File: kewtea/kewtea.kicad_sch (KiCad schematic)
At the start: 61 parts, among them U1 Nice_Nano_V2

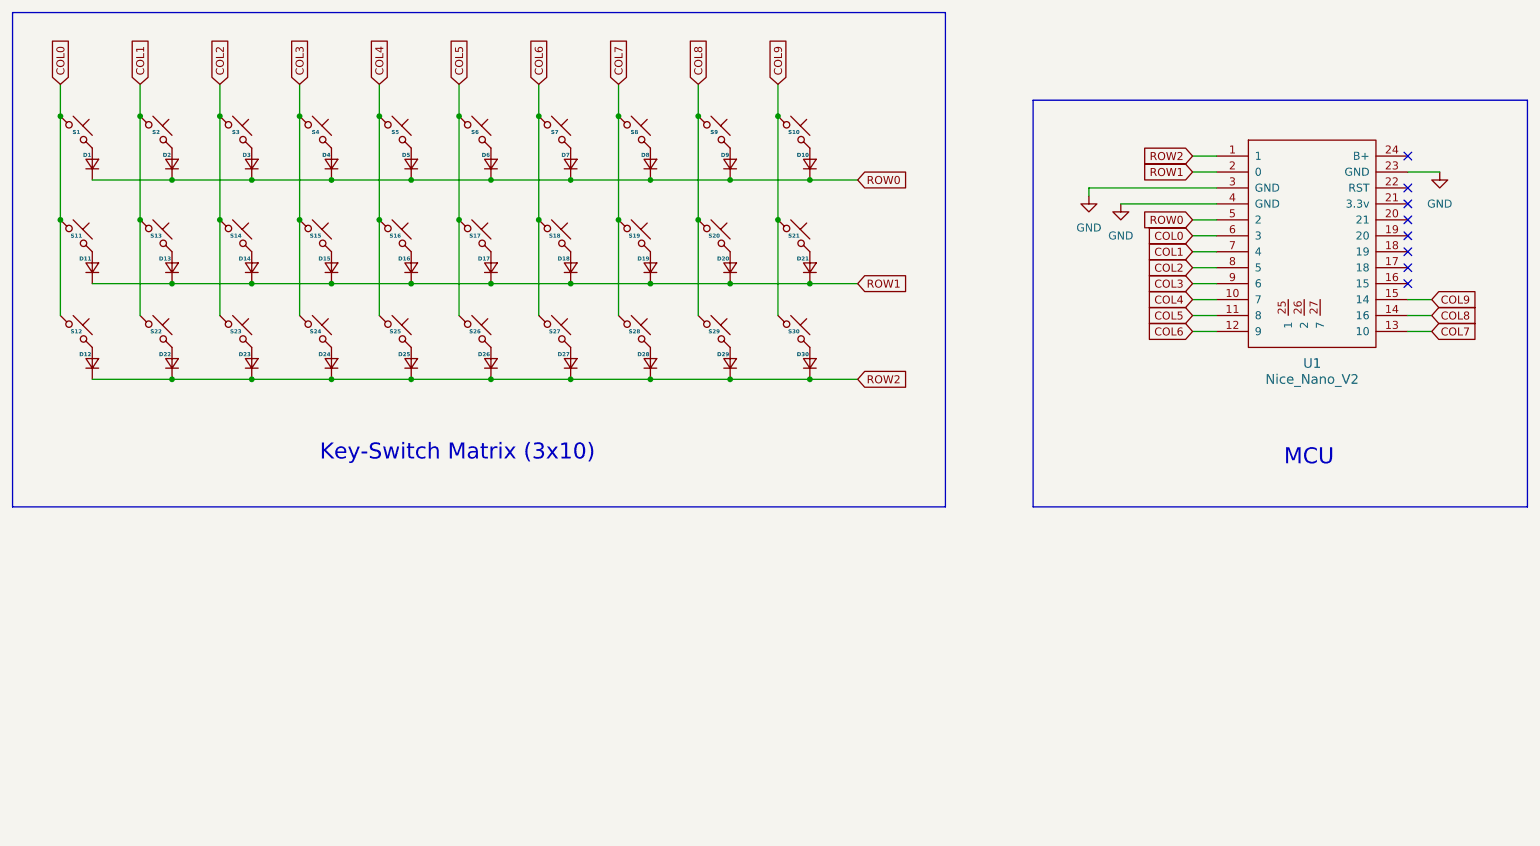
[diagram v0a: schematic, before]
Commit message: add pcb with 3d renders
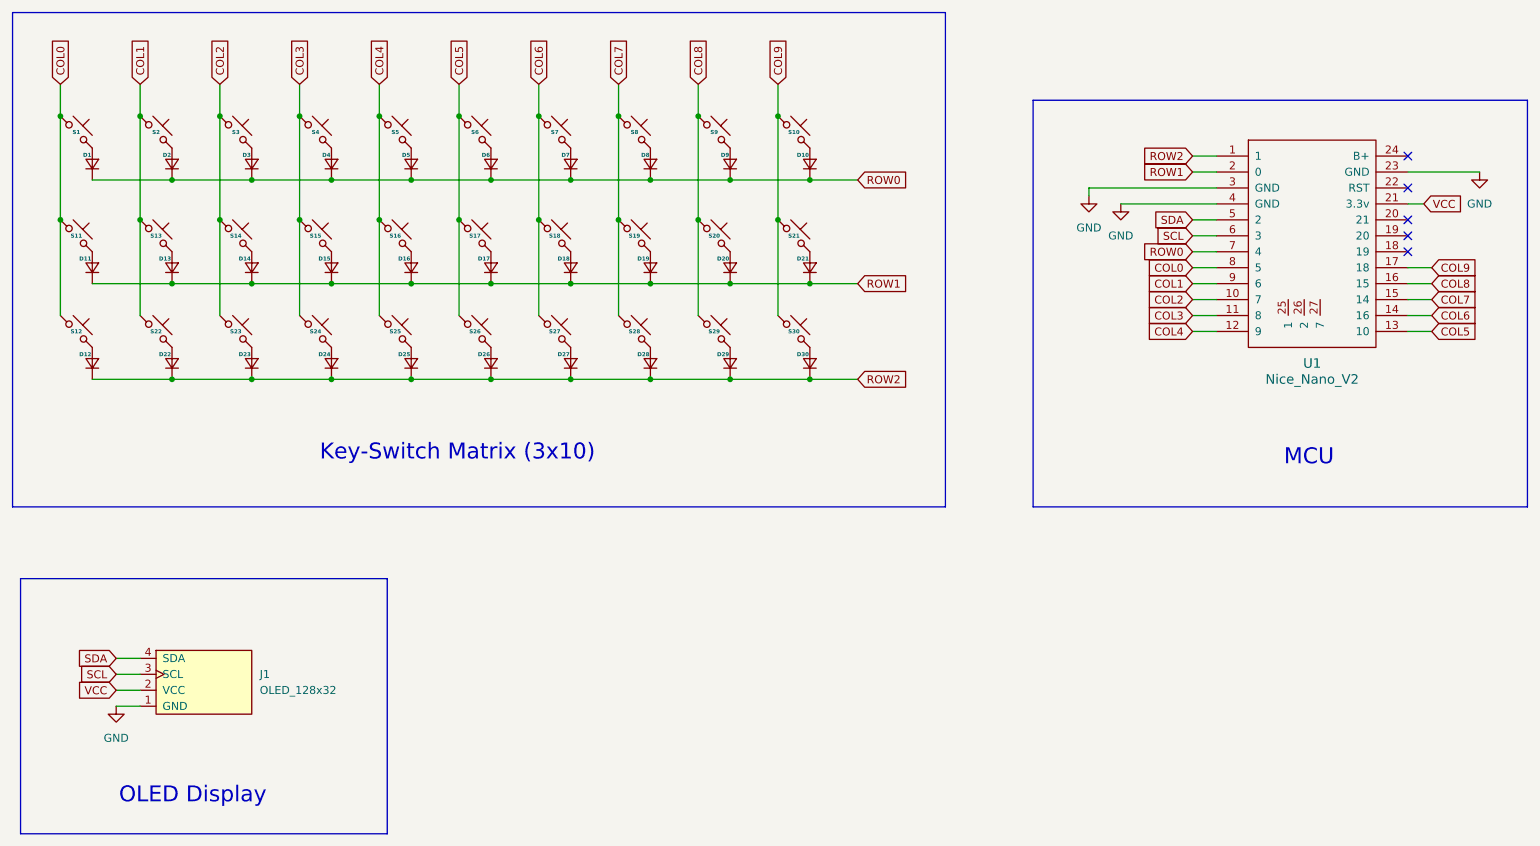
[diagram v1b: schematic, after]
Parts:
- added J1: OLED_128x32, ScottoKeebs_Components:OLED_128x32, symbol ScottoKeebs:OLED_128x32
- D1, D10, D11, D12, D13, D14, D15, D16, D17, D18, D19, D2, D20, D21, D22, D23, D24, D25, D26, D27, D28, D29, D3, D30, D4, D5, D6, D7, D8, D9: footprint (none) -> ScottoKeebs_Components:Diode_DO-35
- S1, S10, S11, S12, S13, S14, S15, S16, S17, S18, S19, S2, S20, S21, S22, S23, S24, S25, S26, S27, S28, S29, S3, S30, S4, S5, S6, S7, S8, S9: footprint (none) -> ScottoKeebs_Choc:Choc_V1
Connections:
- net COL0: now also U1.8 (5); no longer U1.6 (3)
- net COL1: now also U1.9 (6); no longer U1.7 (4)
- net COL2: now also U1.10 (7); no longer U1.8 (5)
- net COL3: now also U1.11 (8); no longer U1.9 (6)
- net COL4: now also U1.12 (9); no longer U1.10 (7)
- net COL5: now also U1.13 (10); no longer U1.11 (8)
- net COL6: now also U1.14 (16); no longer U1.12 (9)
- net COL7: now also U1.15 (14); no longer U1.13 (10)
- net COL8: now also U1.16 (15); no longer U1.14 (16)
- net COL9: now also U1.17 (18); no longer U1.15 (14)
- net GND: now also J1.1 (GND)
- net ROW0: now also U1.7 (4); no longer U1.5 (2)
- net VCC: now reaches U1.21 (3.3v)
- net VCC: now also J1.2 (VCC)
- new net SCL: J1.3 (SCL), U1.6 (3)
- new net SDA: J1.4 (SDA), U1.5 (2)
- no-connect marks 8 -> 5
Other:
- note added: "OLED Display"
